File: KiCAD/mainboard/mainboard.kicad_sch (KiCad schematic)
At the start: 1 part, among them IC1 DLPC1438ZEZ

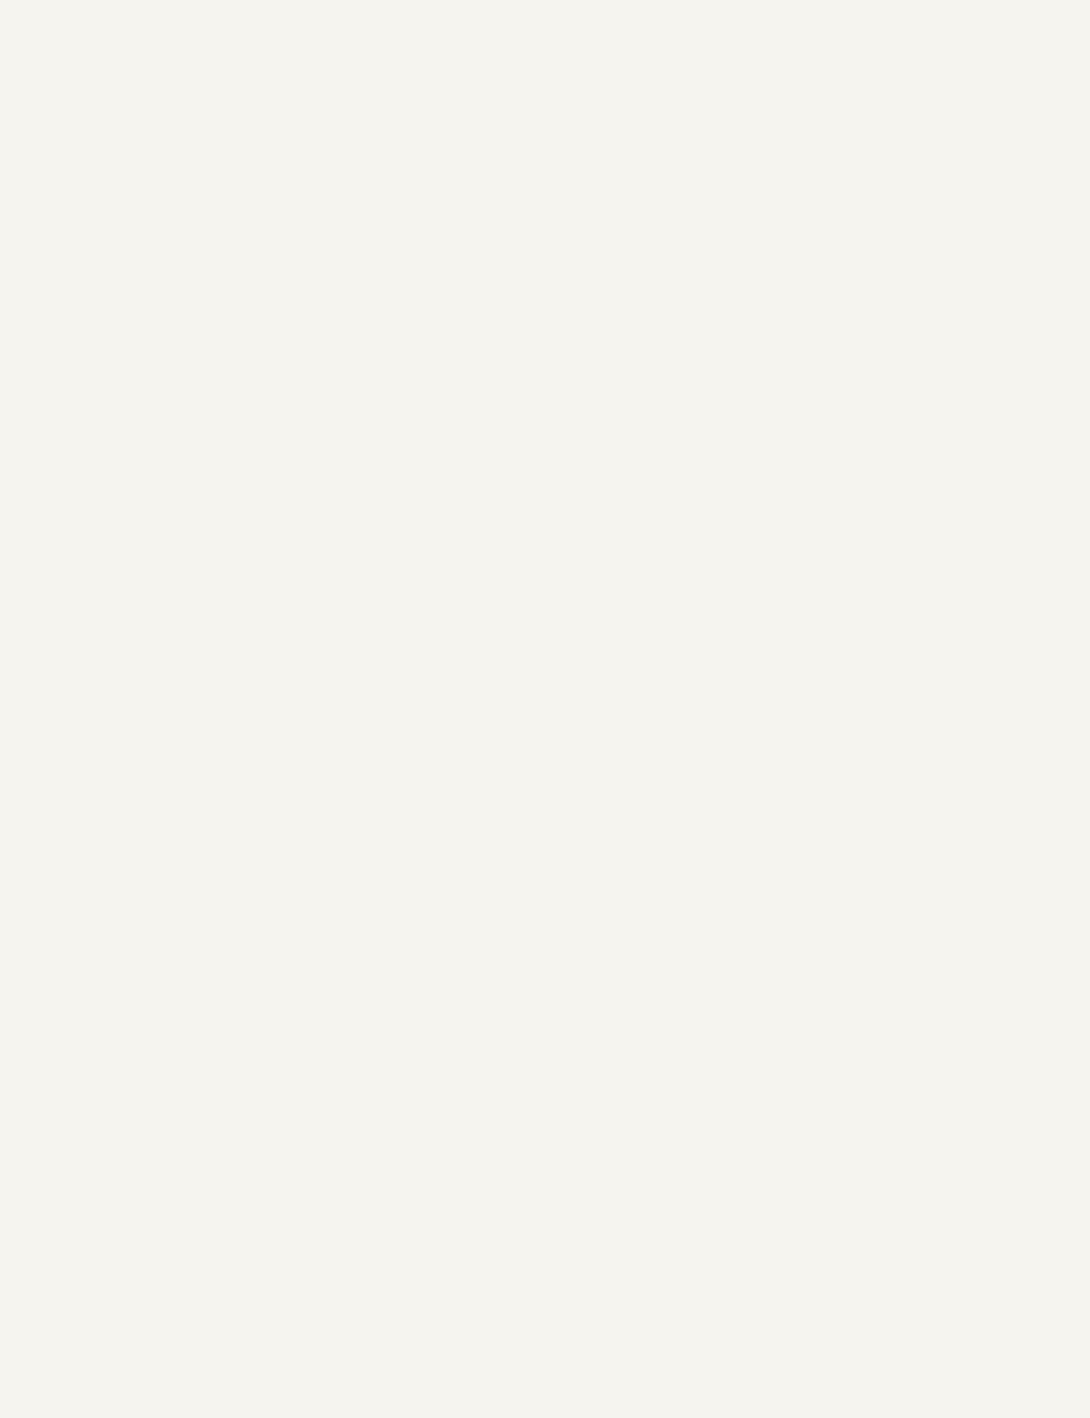
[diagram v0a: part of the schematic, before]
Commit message: dlpa2005 symbol + footprint added to proj specific library
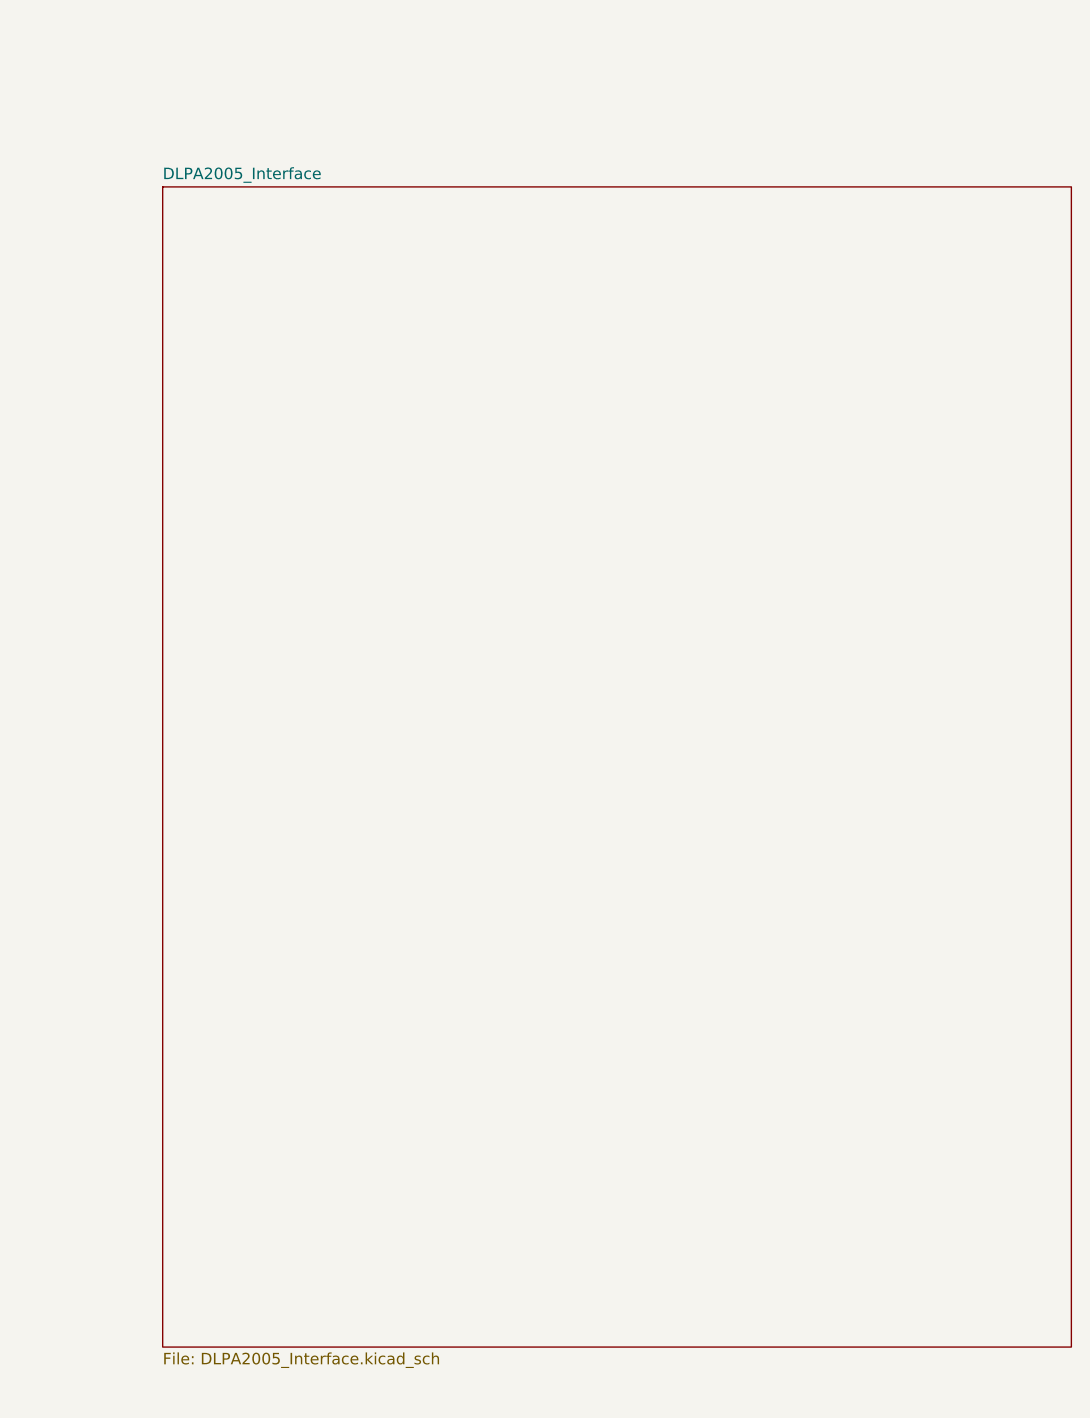
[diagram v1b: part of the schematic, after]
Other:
- added sheet DLPA2005_Interface (DLPA2005_Interface.kicad_sch)
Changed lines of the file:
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@@
+		)
+	)
+	(sheet
+		(at 560.705 176.53)
+		(size 100.965 128.905)
+		(exclude_from_sim no)
+		(in_bom yes)
+		(on_board yes)
+		(dnp no)
+		(fields_autoplaced yes)
+		(stroke
+			(width 0.1524)
+			(type solid)
+		)
+		(fill
+			(color 0 0 0 0.0000)
+		)
+		(property "Sheetname" "DLPA2005_Interface"
+			(at 560.705 175.8184 0)
+			(effects
+				(font
+					(size 1.27 1.27)
+				)
+				(justify left bottom)
+			)
+		)
+		(property "Sheetfile" "DLPA2005_Interface.kicad_sch"
+			(at 560.705 306.0196 0)
+			(effects
+				(font
+					(size 1.27 1.27)
+				)
+				(justify left top)
+			)
+		)
+		(instances
+			(project "mainboard"
+				(path "/38e83f42-2cf9-4799-a46f-ca415d95b90a"
+					(page "2")
+				)
+			)
 		)
 	)

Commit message: some doofus goofus
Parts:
- removed IC1: DLPC1438ZEZ, tp_library:BGA201C80P15X15_1300X1300X100, symbol tp_library:DLPC1438ZEZ
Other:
- added sheet DLPC1438_Interface (DLPC1438_Interface.kicad_sch)
- added sheet DMD_Interface (DMD_Interface.kicad_sch)

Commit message: Val's edit
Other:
- sheet DLPA2005_Interface ports: added RESETZ; removed none
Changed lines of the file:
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@@
+			)
+		)
+		(pin "RESETZ" input
+			(at 673.735 152.4 180)
+			(effects
+				(font
+					(size 1.27 1.27)
+				)
+				(justify left)
 			)
 		)

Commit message: dmd interface done!
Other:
- sheet DLPC1438_Interface ports: added DMD_DEN_ARSTZ, DMD_HS_CLK_N, DMD_HS_CLK_P, DMD_HS_WDATAA_N, DMD_HS_WDATAA_P, DMD_HS_WDATAB_N, DMD_HS_WDATAB_P, DMD_HS_WDATAC_N, DMD_HS_WDATAC_P, DMD_HS_WDATAD_N, DMD_HS_WDATAD_P, DMD_HS_WDATAE_N, DMD_HS_WDATAE_P, DMD_HS_WDATAF_N, DMD_HS_WDATAF_P, DMD_HS_WDATAG_N, DMD_HS_WDATAG_P, DMD_HS_WDATAH_N, DMD_HS_WDATAH_P, DMD_LS_RDATA, FPGA_RDY, LS_CLK, LS_WDATA, PROJ_ON, RC_CHARGE, THERM_PWR; removed none
- sheet DMD_Interface ports: added DMD_DEN_ARSTZ, DMD_HS_CLK_N, DMD_HS_CLK_P, DMD_HS_WDATAA_N, DMD_HS_WDATAA_P, DMD_HS_WDATAB_N, DMD_HS_WDATAB_P, DMD_HS_WDATAC_N, DMD_HS_WDATAC_P, DMD_HS_WDATAD_N, DMD_HS_WDATAD_P, DMD_HS_WDATAE_N, DMD_HS_WDATAE_P, DMD_HS_WDATAF_N, DMD_HS_WDATAF_P, DMD_HS_WDATAG_N, DMD_HS_WDATAG_P, DMD_HS_WDATAH_N, DMD_HS_WDATAH_P, DMD_LS_CLK, DMD_LS_RDATA, DMD_LS_WDATA, PRINT_ACTIVE, SYS_RDY, VBIAS, VOFS, VRST; removed none

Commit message: some new schematics
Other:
- added sheet Power_Input&Generation (power_input&generation.kicad_sch)
- sheet DLPA2005_Interface: file DLPA2005_Interface.kicad_sch -> dlpa2005_Interface.kicad_sch
- sheet DLPC1438_Interface: file DLPC1438_Interface.kicad_sch -> dlpc1438_interface.kicad_sch
- sheet DMD_Interface: file DMD_Interface.kicad_sch -> dmd_interface.kicad_sch
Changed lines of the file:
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@@
+	)
+	(sheet
+		(at 353.06 285.75)
+		(size 73.66 36.83)
+		(exclude_from_sim no)
+		(in_bom yes)
+		(on_board yes)
+		(dnp no)
+		(fields_autoplaced yes)
+		(stroke
+			(width 0.1524)
+			(type solid)
+		)
+		(fill
+			(color 0 0 0 0.0000)
+		)
+		(property "Sheetname" "Power_Input&Generation"
+			(at 353.06 285.0384 0)
+			(effects
+				(font
+					(size 1.27 1.27)
+				)
+				(justify left bottom)
+			)
+		)
+		(property "Sheetfile" "power_input&generation.kicad_sch"
+			(at 353.06 323.1646 0)
+			(effects
+				(font
+					(size 1.27 1.27)
+				)
+				(justify left top)
+			)
+		)
+		(instances
+			(project "mainboard"
+				(path "/38e83f42-2cf9-4799-a46f-ca415d95b90a"
+					(page "5")
+				)
+			)
+		)
 	)
 	(sheet
@@
 			)
 		)
-		(property "Sheetfile" "DMD_Interface.kicad_sch"
+		(property "Sheetfile" "dmd_interface.kicad_sch"
 			(at 123.19 320.6246 0)
 			(effects
@@
 			)
 		)
-		(property "Sheetfile" "DLPA2005_Interface.kicad_sch"
+		(property "Sheetfile" "dlpa2005_Interface.kicad_sch"
 			(at 673.735 232.3596 0)
 			(effects
@@
 			)
 		)
-		(property "Sheetfile" "DLPC1438_Interface.kicad_sch"
+		(property "Sheetfile" "dlpc1438_interface.kicad_sch"
 			(at 121.92 273.6346 0)
 			(effects

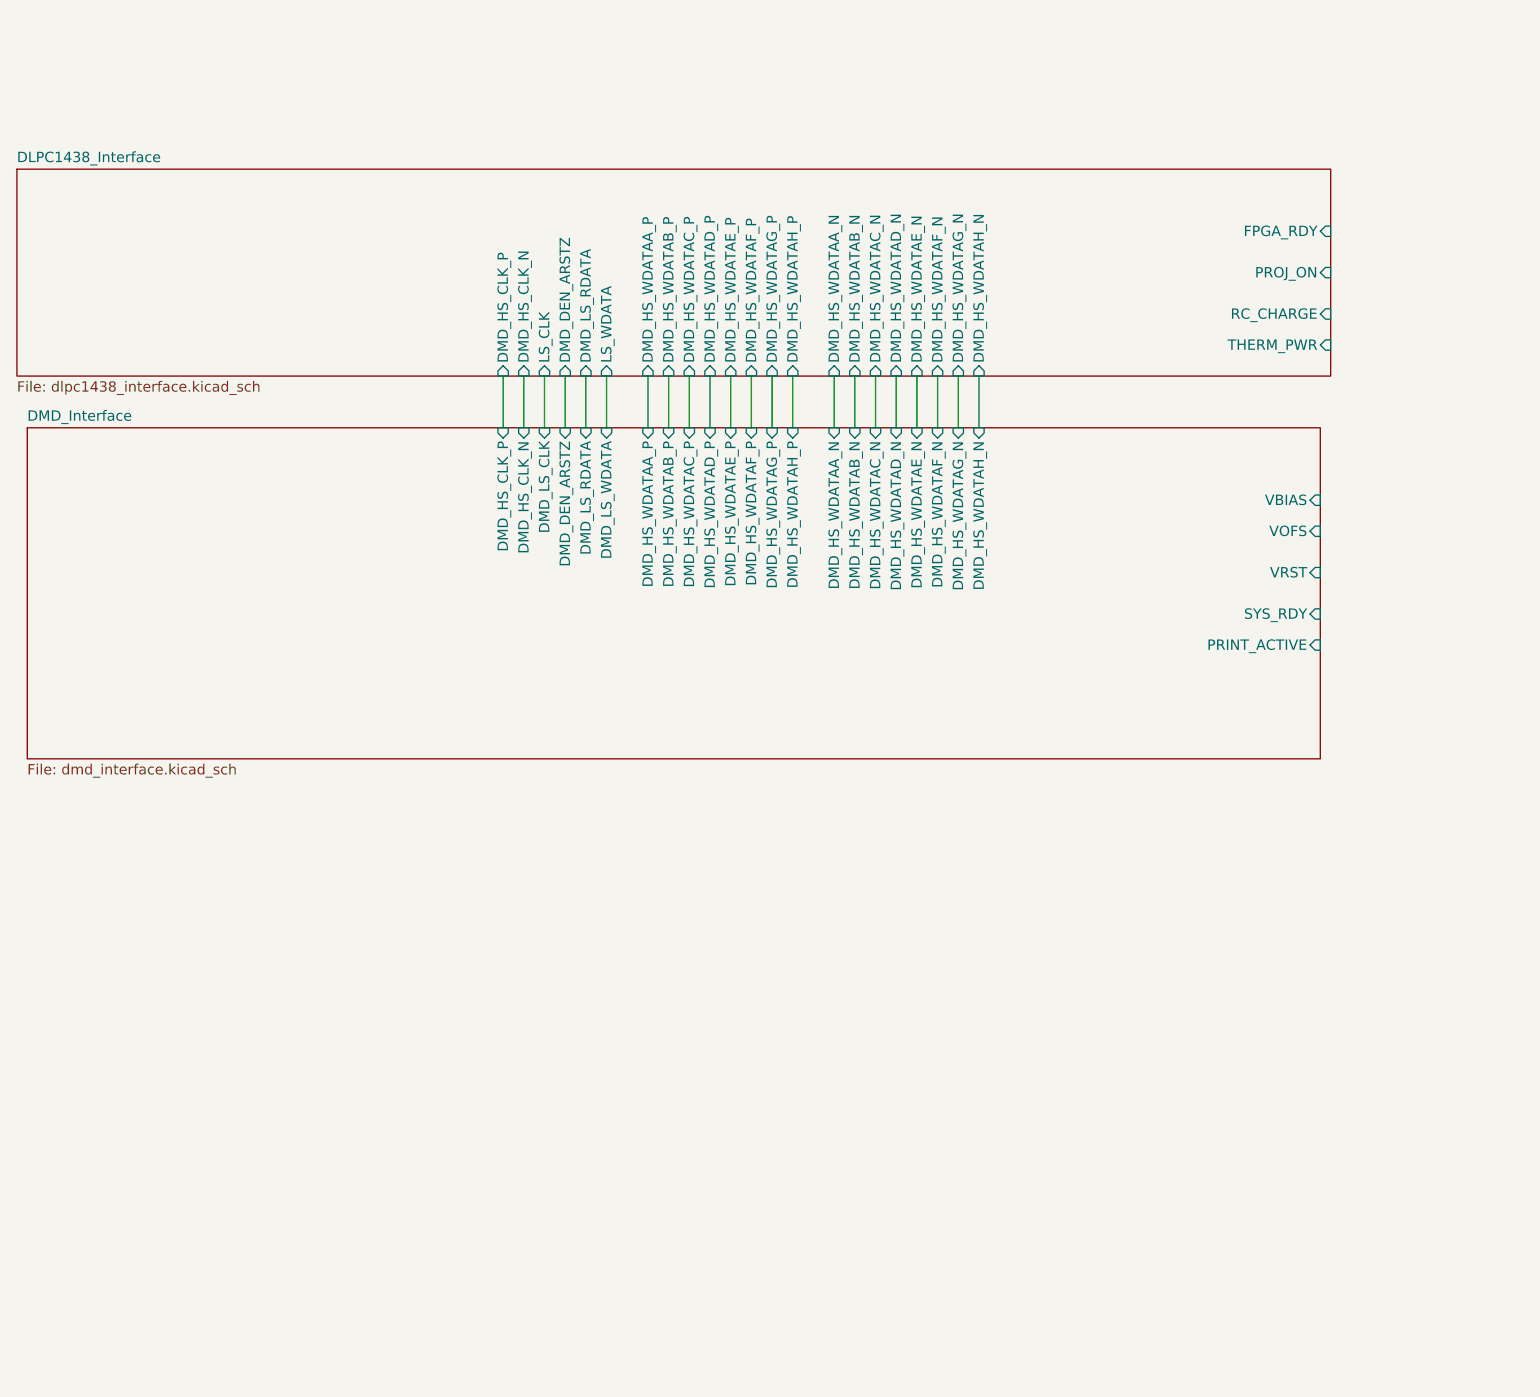
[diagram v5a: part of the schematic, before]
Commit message: WIP dmd interface; made assembly for DMD, started new board for DMD interconnect
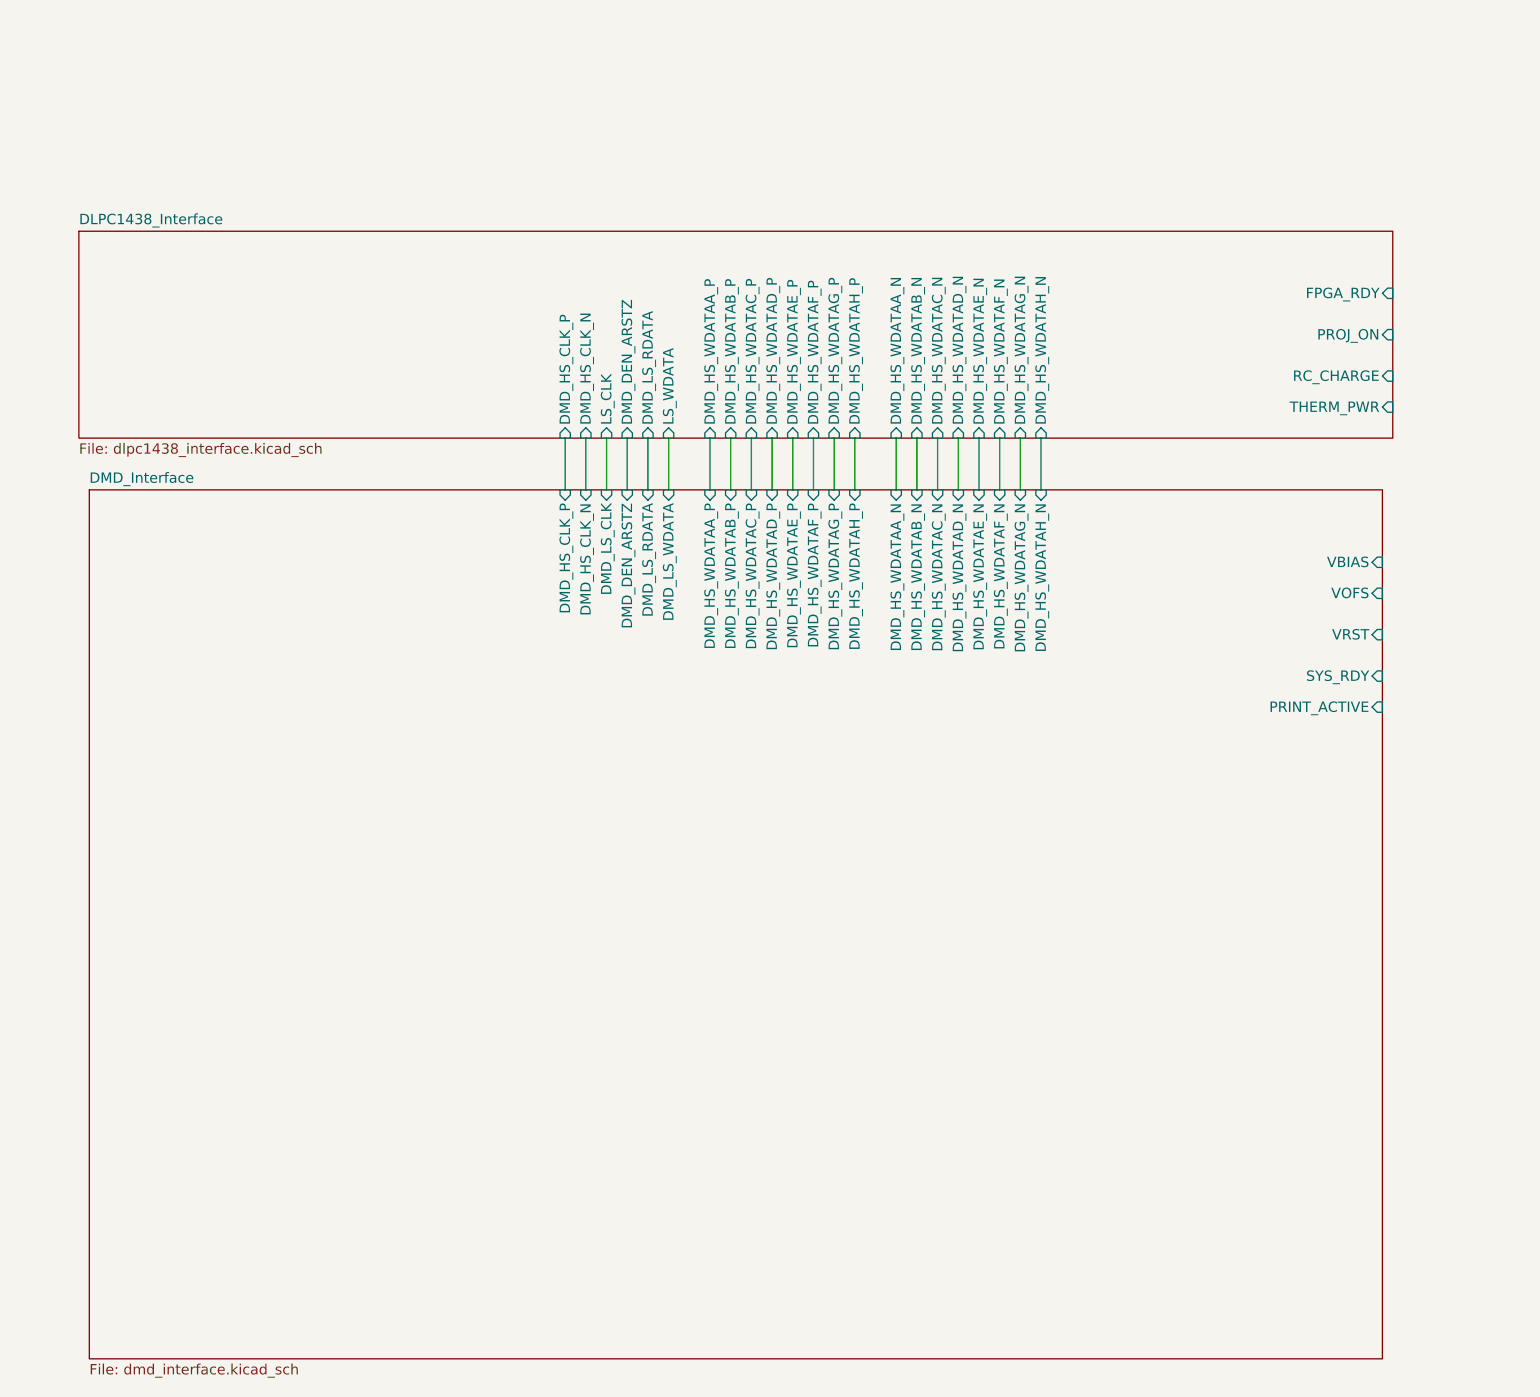
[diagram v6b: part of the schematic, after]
